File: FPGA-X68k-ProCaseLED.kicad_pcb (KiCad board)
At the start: 2 copper layers, 80 x 36 mm, 47 parts, among them J1 Conn_01x05_Male, SW1 SW_DIP_x04, U1 TLC59116IPWR

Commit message: First version
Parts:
- added TP25: RESET, TestPoint:TestPoint_THTPad_D1.5mm_Drill0.7mm, B.Cu at (83.8, 102.2)
- added TP26: SCL, TestPoint:TestPoint_THTPad_D1.5mm_Drill0.7mm, B.Cu at (80.0, 102.2)
- added TP27: SDA, TestPoint:TestPoint_THTPad_D1.5mm_Drill0.7mm, B.Cu at (76.2, 102.2)
- TP24: value +3.3V -> +3V3
- moved H4 0.99 mm to (135.9, 121.9)
- moved H3 0.90 mm to (135.9, 94.0)
- moved TP10 0.64 mm to (133.3, 105.4)
- moved TP2 0.64 mm to (133.3, 118.1)
- moved TP3 0.64 mm to (133.3, 115.6)
- moved TP4 0.64 mm to (133.3, 113.0)
- moved TP5 0.64 mm to (133.3, 102.9)
- moved TP6 0.64 mm to (133.3, 100.3)
- moved TP7 0.64 mm to (133.3, 97.8)
- moved TP8 0.64 mm to (133.3, 110.5)
- moved TP9 0.64 mm to (133.3, 108.0)
- moved H1 0.64 mm to (63.5, 121.9)
- moved J1 0.59 mm to (69.8, 94.1)
- moved H2 0.57 mm to (76.8, 94.0)
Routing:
- net /RESET: track 49.0 -> 62.0 mm
- net /SCL: track 48.3 -> 59.3 mm
- net /SDA: track 46.9 -> 52.9 mm
- net +3V3: track 162.2 -> 160.7 mm
- net /TIMER_LED_B: track 5.38 -> 6.69 mm
- net /POWER_LED_B: track 49.9 -> 48.6 mm
- net /HD_BUSY_LED_G: track 34.7 -> 33.4 mm
- net /TIMER_LED_R: track 33.3 -> 32.6 mm
- net /TIMER_LED_G: track 4.42 -> 3.78 mm
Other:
- board size 80 x 36 mm -> 79.5 x 35 mm

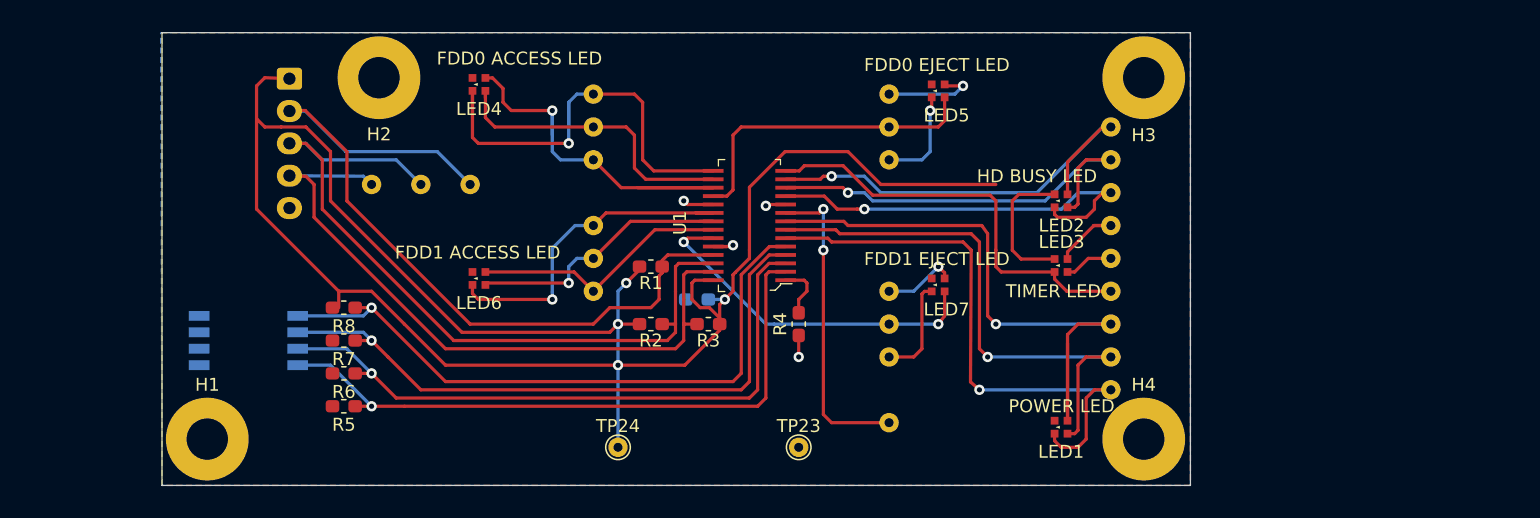
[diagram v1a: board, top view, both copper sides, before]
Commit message: Add miniature FDD sensor circuit.
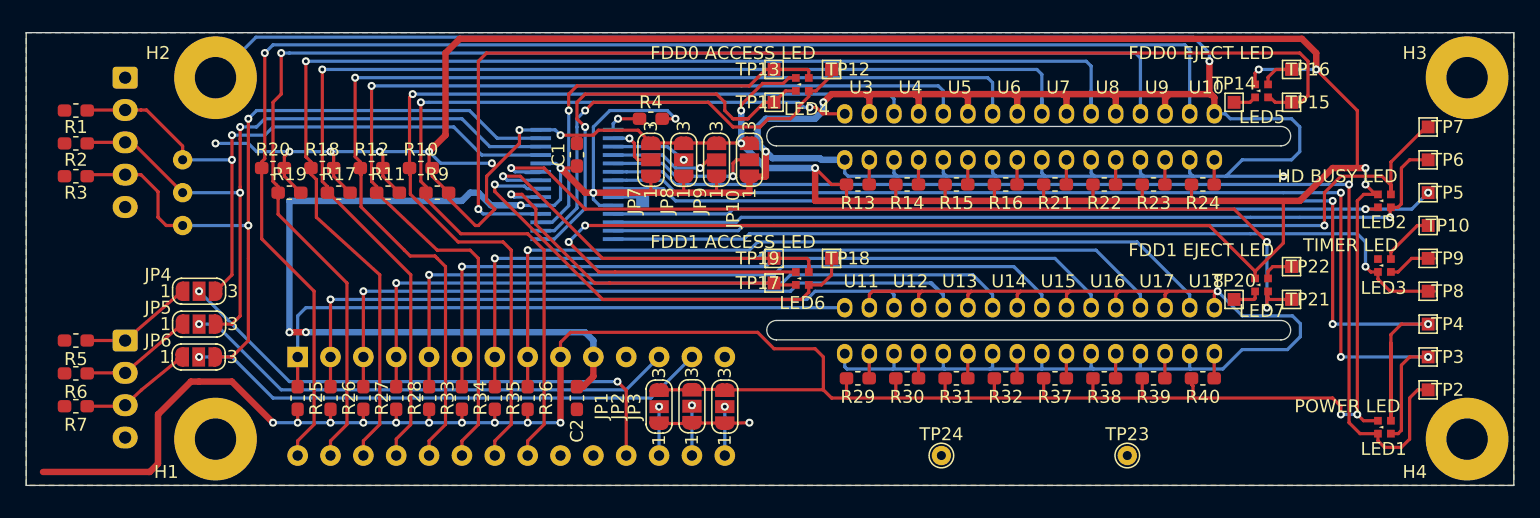
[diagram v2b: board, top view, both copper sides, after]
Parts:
- removed R8: 4K7, Resistor_SMD:R_0603_1608Metric_Pad1.05x0.95mm_HandSolder
- removed SW1: SW_DIP_x04, Button_Switch_SMD:SW_DIP_SPSTx04_Slide_Copal_CHS-04B_W7.62mm_P1.27mm
- added C2: C_Small, Capacitor_SMD:C_0603_1608Metric_Pad1.05x0.95mm_HandSolder, F.Cu at (92.1, 118.7)
- added J2: Conn_01x04_Male, Connector_JST:JST_EH_S4B-EH_1x04_P2.50mm_Horizontal, B.Cu at (57.1, 114.3)
- added JP1: JUMPER3, Jumper:SolderJumper-3_P1.3mm_Open_RoundedPad1.0x1.5mm_NumberLabels, F.Cu at (98.4, 119.4)
- added JP10: JUMPER3, Jumper:SolderJumper-3_P1.3mm_Open_RoundedPad1.0x1.5mm_NumberLabels, F.Cu at (105.4, 100.3)
- added JP2: JUMPER3, Jumper:SolderJumper-3_P1.3mm_Open_RoundedPad1.0x1.5mm_NumberLabels, F.Cu at (101.0, 119.4)
- added JP3: JUMPER3, Jumper:SolderJumper-3_P1.3mm_Open_RoundedPad1.0x1.5mm_NumberLabels, F.Cu at (103.5, 119.4)
- added JP4: JUMPER3, Jumper:SolderJumper-3_P1.3mm_Open_RoundedPad1.0x1.5mm_NumberLabels, F.Cu at (62.9, 110.5)
- added JP5: JUMPER3, Jumper:SolderJumper-3_P1.3mm_Open_RoundedPad1.0x1.5mm_NumberLabels, F.Cu at (62.9, 113.0)
- added JP6: JUMPER3, Jumper:SolderJumper-3_P1.3mm_Open_RoundedPad1.0x1.5mm_NumberLabels, F.Cu at (62.8, 115.6)
- added JP7: JUMPER3, Jumper:SolderJumper-3_P1.3mm_Open_RoundedPad1.0x1.5mm_NumberLabels, F.Cu at (97.8, 100.3)
- added JP8: JUMPER3, Jumper:SolderJumper-3_P1.3mm_Open_RoundedPad1.0x1.5mm_NumberLabels, F.Cu at (100.3, 100.3)
- added JP9: JUMPER3, Jumper:SolderJumper-3_P1.3mm_Open_RoundedPad1.0x1.5mm_NumberLabels, F.Cu at (102.9, 100.3)
- added R10: 4K7, Resistor_SMD:R_0603_1608Metric_Pad1.05x0.95mm_HandSolder, F.Cu at (80.0, 101.0)
- added R11: 4K7, Resistor_SMD:R_0603_1608Metric_Pad1.05x0.95mm_HandSolder, F.Cu at (77.5, 102.9)
- added R12: 4K7, Resistor_SMD:R_0603_1608Metric_Pad1.05x0.95mm_HandSolder, F.Cu at (76.2, 101.0)
- added R13: 510, Resistor_SMD:R_0603_1608Metric_Pad1.05x0.95mm_HandSolder, F.Cu at (113.8, 102.2)
- added R14: 510, Resistor_SMD:R_0603_1608Metric_Pad1.05x0.95mm_HandSolder, F.Cu at (117.6, 102.2)
- added R15: 510, Resistor_SMD:R_0603_1608Metric_Pad1.05x0.95mm_HandSolder, F.Cu at (121.4, 102.2)
- added R16: 510, Resistor_SMD:R_0603_1608Metric_Pad1.05x0.95mm_HandSolder, F.Cu at (125.2, 102.2)
- added R17: 4K7, Resistor_SMD:R_0603_1608Metric_Pad1.05x0.95mm_HandSolder, F.Cu at (73.7, 102.9)
- added R18: 4K7, Resistor_SMD:R_0603_1608Metric_Pad1.05x0.95mm_HandSolder, F.Cu at (72.4, 101.0)
- added R19: 4K7, Resistor_SMD:R_0603_1608Metric_Pad1.05x0.95mm_HandSolder, F.Cu at (69.8, 102.9)
- added R20: 4K7, Resistor_SMD:R_0603_1608Metric_Pad1.05x0.95mm_HandSolder, F.Cu at (68.6, 101.0)
- added R21: 510, Resistor_SMD:R_0603_1608Metric_Pad1.05x0.95mm_HandSolder, F.Cu at (129.0, 102.2)
- added R22: 510, Resistor_SMD:R_0603_1608Metric_Pad1.05x0.95mm_HandSolder, F.Cu at (132.8, 102.2)
- added R23: 510, Resistor_SMD:R_0603_1608Metric_Pad1.05x0.95mm_HandSolder, F.Cu at (136.7, 102.2)
- added R24: 510, Resistor_SMD:R_0603_1608Metric_Pad1.05x0.95mm_HandSolder, F.Cu at (140.5, 102.2)
- added R25: 4K7, Resistor_SMD:R_0603_1608Metric_Pad1.05x0.95mm_HandSolder, F.Cu at (70.5, 118.7)
- added R26: 4K7, Resistor_SMD:R_0603_1608Metric_Pad1.05x0.95mm_HandSolder, F.Cu at (73.0, 118.7)
- added R27: 4K7, Resistor_SMD:R_0603_1608Metric_Pad1.05x0.95mm_HandSolder, F.Cu at (75.6, 118.7)
- added R28: 4K7, Resistor_SMD:R_0603_1608Metric_Pad1.05x0.95mm_HandSolder, F.Cu at (78.1, 118.7)
- added R29: 510, Resistor_SMD:R_0603_1608Metric_Pad1.05x0.95mm_HandSolder, F.Cu at (113.8, 117.2)
- added R30: 510, Resistor_SMD:R_0603_1608Metric_Pad1.05x0.95mm_HandSolder, F.Cu at (117.6, 117.2)
- added R31: 510, Resistor_SMD:R_0603_1608Metric_Pad1.05x0.95mm_HandSolder, F.Cu at (121.4, 117.2)
- added R32: 510, Resistor_SMD:R_0603_1608Metric_Pad1.05x0.95mm_HandSolder, F.Cu at (125.2, 117.2)
- added R33: 4K7, Resistor_SMD:R_0603_1608Metric_Pad1.05x0.95mm_HandSolder, F.Cu at (80.6, 118.7)
- added R34: 4K7, Resistor_SMD:R_0603_1608Metric_Pad1.05x0.95mm_HandSolder, F.Cu at (83.2, 118.7)
- added R35: 4K7, Resistor_SMD:R_0603_1608Metric_Pad1.05x0.95mm_HandSolder, F.Cu at (85.7, 118.7)
- added R36: 4K7, Resistor_SMD:R_0603_1608Metric_Pad1.05x0.95mm_HandSolder, F.Cu at (88.3, 118.7)
- added R37: 510, Resistor_SMD:R_0603_1608Metric_Pad1.05x0.95mm_HandSolder, F.Cu at (129.0, 117.2)
- added R38: 510, Resistor_SMD:R_0603_1608Metric_Pad1.05x0.95mm_HandSolder, F.Cu at (132.8, 117.2)
- added R39: 510, Resistor_SMD:R_0603_1608Metric_Pad1.05x0.95mm_HandSolder, F.Cu at (136.7, 117.2)
- added R40: 510, Resistor_SMD:R_0603_1608Metric_Pad1.05x0.95mm_HandSolder, F.Cu at (140.5, 117.2)
- added R9: 4K7, Resistor_SMD:R_0603_1608Metric_Pad1.05x0.95mm_HandSolder, F.Cu at (81.3, 102.9)
- added U10: TPR-105, local:TPR-105, F.Cu at (140.7, 94.2)
- added U11: TPR-105, local:TPR-105, F.Cu at (114.0, 109.2)
- added U12: TPR-105, local:TPR-105, F.Cu at (117.9, 109.2)
- added U13: TPR-105, local:TPR-105, F.Cu at (121.7, 109.2)
- added U14: TPR-105, local:TPR-105, F.Cu at (125.5, 109.2)
- added U15: TPR-105, local:TPR-105, F.Cu at (129.3, 109.2)
- added U16: TPR-105, local:TPR-105, F.Cu at (133.1, 109.2)
- added U17: TPR-105, local:TPR-105, F.Cu at (136.9, 109.2)
- added U18: TPR-105, local:TPR-105, F.Cu at (140.7, 109.2)
- added U2: MCP23017_SP, Package_DIP:DIP-28_W7.62mm, B.Cu at (70.5, 115.6)
- added U3: TPR-105, local:TPR-105, F.Cu at (114.0, 94.2)
- added U4: TPR-105, local:TPR-105, F.Cu at (117.9, 94.2)
- added U5: TPR-105, local:TPR-105, F.Cu at (121.7, 94.2)
- added U6: TPR-105, local:TPR-105, F.Cu at (125.5, 94.2)
- added U7: TPR-105, local:TPR-105, F.Cu at (129.3, 94.2)
- added U8: TPR-105, local:TPR-105, F.Cu at (133.1, 94.2)
- added U9: TPR-105, local:TPR-105, F.Cu at (136.9, 94.2)
- C1: moved to F.Cu
- TP1: footprint TestPoint:TestPoint_THTPad_D1.5mm_Drill0.7mm -> TestPoint:TestPoint_Pad_1.0x1.0mm
- TP10, TP11, TP12, TP13, TP14, TP15, TP16, TP17, TP18, TP19, TP2, TP20, TP21, TP22, TP3, TP4, TP5, TP6, TP7, TP8, TP9: footprint TestPoint:TestPoint_THTPad_D1.5mm_Drill0.7mm -> TestPoint:TestPoint_Pad_1.0x1.0mm; moved to F.Cu
- TP24: value +3V3 -> +3.3V
- U1: moved to B.Cu
- moved R3 50.2 mm to (53.3, 101.6), turned to 180 degrees
- moved R2 46.6 mm to (53.3, 99.1)
- moved R1 46.1 mm to (53.3, 96.5)
- moved TP15 31.2 mm to (147.3, 95.9)
- moved TP16 31.2 mm to (147.3, 93.3)
- moved TP21 31.2 mm to (147.3, 111.1)
- moved TP22 31.2 mm to (147.3, 108.6)
- moved TP14 27.0 mm to (142.9, 95.9)
- moved TP20 27.0 mm to (142.9, 111.1)
- moved TP1 25.6 mm to (97.2, 103.5)
- moved TP23 25.4 mm to (134.6, 123.2)
- moved TP24 25.0 mm to (120.2, 123.2)
- moved H3 25.0 mm to (160.9, 94.0)
- moved H4 25.0 mm to (160.9, 121.9)
- moved LED1 25.0 mm to (154.5, 121.0)
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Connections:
- R5 pad 1: Net-(R5-Pad1) -> Net-(J2-Pad1)
- R6 pad 1: Net-(R6-Pad1) -> Net-(J2-Pad2)
- R7 pad 1: Net-(R7-Pad1) -> Net-(J2-Pad3)
- U1 pad 2: Net-(R5-Pad1) -> Net-(JP7-Pad2)
- U1 pad 3: Net-(R6-Pad1) -> Net-(JP8-Pad2)
- U1 pad 4: Net-(R7-Pad1) -> Net-(JP9-Pad2)
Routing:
- net GND: track 9.61 -> 447.7 mm, vias 4 -> 12
- net +3V3: track 160.7 -> 526.9 mm, vias 4 -> 29
- net /FD0ID7: track 0.00 -> 110.5 mm, vias 0 -> 1
- net /FD0ID6: track 0.00 -> 105.8 mm, vias 0 -> 1
- net /FD0ID5: track 0.00 -> 100.0 mm, vias 0 -> 1
- net /FD0ID4: track 0.00 -> 93.4 mm, vias 0 -> 1
- net /FD0ID3: track 0.00 -> 85.8 mm, vias 0 -> 1
- net /FD0ID2: track 0.00 -> 80.2 mm, vias 0 -> 1
- net /FD0ID1: track 0.00 -> 72.4 mm, vias 0 -> 1
- net /FD0ID0: track 0.00 -> 68.1 mm, vias 0 -> 2
- net /FD1ID7: track 0.00 -> 64.7 mm, vias 0 -> 1
- net /FDD0_EJECT_G: track 24.6 -> 87.2 mm, vias 0 -> 1
- net /FD1ID6: track 0.00 -> 62.5 mm, vias 0 -> 1
- net /FD1ID5: track 0.00 -> 60.4 mm, vias 0 -> 1
- net /FD1ID4: track 0.00 -> 58.2 mm, vias 0 -> 1
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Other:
- board size 79.5 x 35 mm -> 115 x 35 mm
- net class Default: via_dia 0.8 -> 0.62; via_drill 0.4 -> 0.3
- net class Power added: clearance 0.2, trace_width 0.5, via_dia 0.8, via_drill 0.4
- board text added: "LED / FDD Board for FPGA X68000 PRO Case Aug 2020 Kunihiko Ohnaka @kunichiko"
- board text removed: "LED Board for FPGA X68000 PRO Case Aug 2020 Kunihiko Ohnaka @kunichiko"

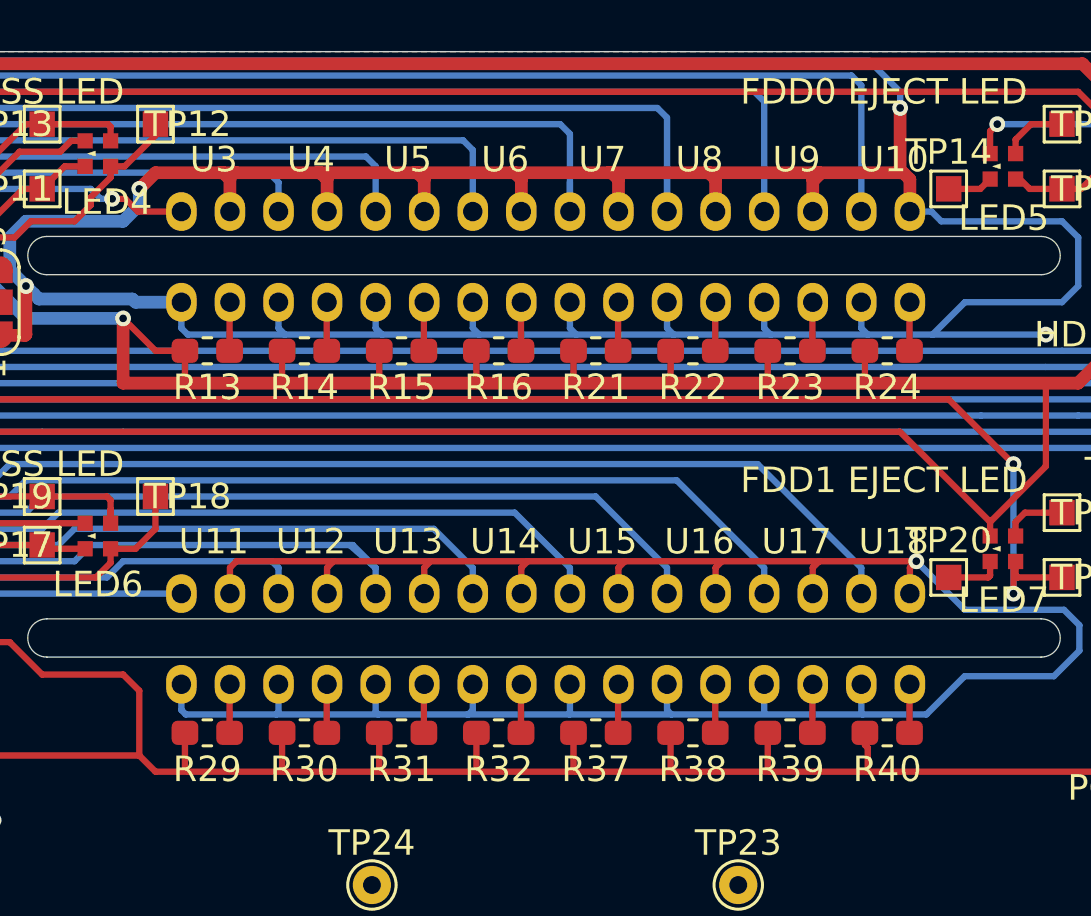
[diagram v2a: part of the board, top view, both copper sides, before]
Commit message: Fix the direction of TPR-105.
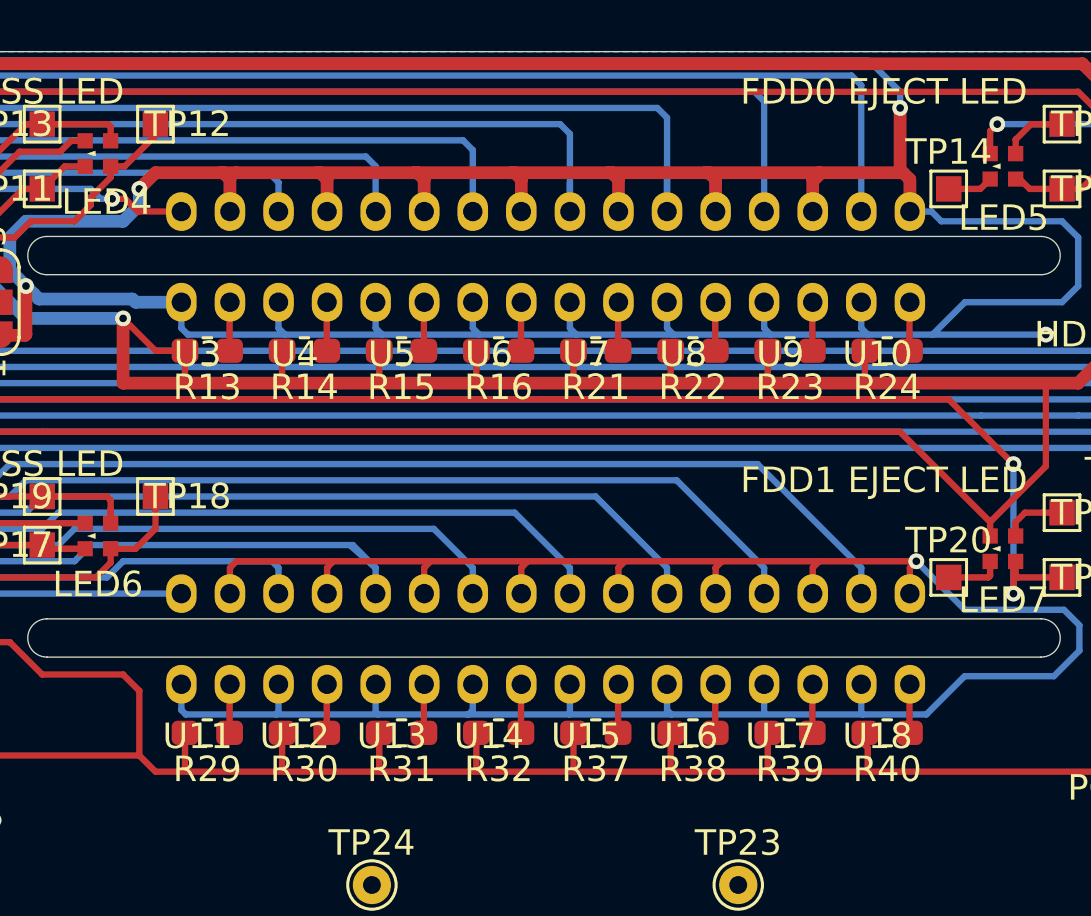
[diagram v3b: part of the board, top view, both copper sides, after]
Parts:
- moved U10 8.66 mm to (140.1, 102.9), turned to 180 degrees
- moved U3 8.66 mm to (113.4, 102.9), turned to 180 degrees
- moved U6 8.66 mm to (124.8, 102.9), turned to 180 degrees
- moved U9 8.66 mm to (136.3, 102.9), turned to 180 degrees
- moved U4 8.66 mm to (117.2, 102.9), turned to 180 degrees
- moved U5 8.66 mm to (121.0, 102.9), turned to 180 degrees
- moved U7 8.66 mm to (128.7, 102.9), turned to 180 degrees
- moved U8 8.66 mm to (132.5, 102.9), turned to 180 degrees
- moved U11 8.66 mm to (113.4, 117.9), turned to 180 degrees
- moved U14 8.66 mm to (124.8, 117.9), turned to 180 degrees
- moved U17 8.66 mm to (136.3, 117.9), turned to 180 degrees
- moved U18 8.66 mm to (140.1, 117.9), turned to 180 degrees
- moved U12 8.66 mm to (117.2, 117.9), turned to 180 degrees
- moved U13 8.66 mm to (121.0, 117.9), turned to 180 degrees
- moved U15 8.66 mm to (128.7, 117.9), turned to 180 degrees
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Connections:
- U10 pad A: /FD0ID7 -> Net-(R24-Pad1)
- U10 pad C: Net-(R24-Pad1) -> /FD0ID7
- U11 pad A: /FD1ID0 -> Net-(R29-Pad1)
- U11 pad C: Net-(R29-Pad1) -> /FD1ID0
- U12 pad A: /FD1ID1 -> Net-(R30-Pad1)
- U12 pad C: Net-(R30-Pad1) -> /FD1ID1
- U13 pad A: /FD1ID2 -> Net-(R31-Pad1)
- U13 pad C: Net-(R31-Pad1) -> /FD1ID2
- U14 pad A: /FD1ID3 -> Net-(R32-Pad1)
- U14 pad C: Net-(R32-Pad1) -> /FD1ID3
- U15 pad A: /FD1ID4 -> Net-(R37-Pad1)
- U15 pad C: Net-(R37-Pad1) -> /FD1ID4
- U16 pad A: /FD1ID5 -> Net-(R38-Pad1)
- U16 pad C: Net-(R38-Pad1) -> /FD1ID5
- U17 pad A: /FD1ID6 -> Net-(R39-Pad1)
- U17 pad C: Net-(R39-Pad1) -> /FD1ID6
- U18 pad A: /FD1ID7 -> Net-(R40-Pad1)
- U18 pad C: Net-(R40-Pad1) -> /FD1ID7
- U3 pad A: /FD0ID0 -> Net-(R13-Pad1)
- U3 pad C: Net-(R13-Pad1) -> /FD0ID0
- U4 pad A: /FD0ID1 -> Net-(R14-Pad1)
- U4 pad C: Net-(R14-Pad1) -> /FD0ID1
- U5 pad A: /FD0ID2 -> Net-(R15-Pad1)
- U5 pad C: Net-(R15-Pad1) -> /FD0ID2
- U6 pad A: /FD0ID3 -> Net-(R16-Pad1)
- U6 pad C: Net-(R16-Pad1) -> /FD0ID3
- U7 pad A: /FD0ID4 -> Net-(R21-Pad1)
- U7 pad C: Net-(R21-Pad1) -> /FD0ID4
- U8 pad A: /FD0ID5 -> Net-(R22-Pad1)
- U8 pad C: Net-(R22-Pad1) -> /FD0ID5
- U9 pad A: /FD0ID6 -> Net-(R23-Pad1)
- U9 pad C: Net-(R23-Pad1) -> /FD0ID6

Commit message: Fix LTSN-B32JEGBB-LY's footprint and TIMER LED pattern.
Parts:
- moved TP14 5.12 mm to (147.3, 93.3)
- moved TP16 5.12 mm to (142.9, 95.9)
- moved TP20 5.12 mm to (147.3, 108.6)
- moved TP22 5.12 mm to (142.9, 111.1)
- moved TP2 5.08 mm to (157.9, 113.0)
- moved TP8 5.08 mm to (157.9, 105.4)
- moved TP10 5.08 mm to (157.9, 110.5)
- moved TP4 5.08 mm to (157.9, 118.1)
- moved TP7 5.08 mm to (157.9, 102.9)
- moved TP5 4.95 mm to (157.9, 97.9)
- moved TP11 2.54 mm to (107.3, 93.3)
- moved TP13 2.54 mm to (107.3, 95.9)
- moved TP19 2.29 mm to (107.3, 110.2)
- moved TP17 1.91 mm to (107.3, 108.0)
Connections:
- U1 pad 11: /HD_BUSY_LED_R -> /HD_BUSY_LED_B
- U1 pad 13: /HD_BUSY_LED_B -> /HD_BUSY_LED_R
- U1 pad 15: /FDD0_ACCESS_R -> /FDD0_ACCESS_B
- U1 pad 17: /FDD0_ACCESS_B -> /FDD0_ACCESS_R
- U1 pad 20: /FDD1_ACCESS_R -> /FDD1_ACCESS_B
- U1 pad 22: /FDD1_ACCESS_B -> /FDD1_ACCESS_R
- U1 pad 6: /POWER_LED_R -> /POWER_LED_B
- U1 pad 8: /POWER_LED_B -> /POWER_LED_R
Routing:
- net /HD_BUSY_LED_R: track 64.7 -> 70.7 mm, vias 2 -> 1
- net /HD_BUSY_LED_B: track 70.7 -> 64.7 mm, vias 1 -> 2
- net /FDD1_ACCESS_B: track 30.9 -> 27.8 mm
- net /FDD1_ACCESS_R: track 28.0 -> 30.9 mm
- net /POWER_LED_R: track 86.6 -> 88.8 mm, vias 1 -> 3
- net /POWER_LED_B: track 88.8 -> 86.6 mm, vias 3 -> 1
- net /FDD0_ACCESS_R: track 33.3 -> 31.3 mm
- net /FDD0_ACCESS_B: track 31.3 -> 33.3 mm
- net /FDD0_EJECT_R: track 1.78 -> 2.62 mm
- net /FDD0_EJECT_B: track 2.62 -> 1.78 mm
- net /TIMER_LED_R: track 66.9 -> 66.2 mm
- net /TIMER_LED_B: track 4.27 -> 4.82 mm
